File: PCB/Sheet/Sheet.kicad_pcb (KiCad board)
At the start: 2 copper layers, 36 x 32.4 mm, 4 parts, among them U1 MCP9700Ax-ELT, U2 MCP2562-E-MF, U3 ATtiny1616-M, U6 MCP2515-xST

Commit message: Update Sheet.kicad_pcb
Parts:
- added R1: R_0201_0603Metric, Resistor_SMD:R_0201_0603Metric, F.Cu at (172.8, 104.6)
- added R2: R_0201_0603Metric, Resistor_SMD:R_0201_0603Metric, F.Cu at (191.1, 104.5)
- added R3: R_0201_0603Metric, Resistor_SMD:R_0201_0603Metric, F.Cu at (193.3, 115.7)
- added R4: R_0201_0603Metric, Resistor_SMD:R_0201_0603Metric, F.Cu at (178.1, 126.5)
- added R5: R_0201_0603Metric, Resistor_SMD:R_0201_0603Metric, F.Cu at (170.5, 116.3)
- added R6: R_0201_0603Metric, Resistor_SMD:R_0201_0603Metric, F.Cu at (181.4, 109.0)
- added adxl335-: Analog_LGA-16_3.25x3mm_P0.5mm_LayoutBorder3x5y, Sensor_Motion:Analog_LGA-16_3.25x3mm_P0.5mm_LayoutBorder3x5y, F.Cu at (177.4, 111.0)
- moved U2 19.6 mm to (193.5, 108.2)
- moved U1 1.85 mm to (190.6, 119.8), turned to 180 degrees
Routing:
- net (no net): track 0.00 -> 208.9 mm, vias 0 -> 6
- net Net-(U1-GND): track 0.00 -> 35.8 mm, vias 0 -> 2
- net Net-(U1-V_{DD}): track 0.00 -> 32.7 mm
- net Net-(U2-RXD): track 0.00 -> 24.4 mm, vias 0 -> 2
- net Net-(U2-TXD): track 0.00 -> 8.92 mm
- net Net-(U1-V_{OUT}): track 0.00 -> 8.76 mm, vias 0 -> 2
- net unconnected-(U2-CANH-Pad7): track 0.00 -> 0.94 mm, vias 0 -> 1
- net unconnected-(U2-CANL-Pad6): track 0.00 -> 0.91 mm, vias 0 -> 1

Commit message: PCB design
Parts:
- removed adxl335-: Analog_LGA-16_3.25x3mm_P0.5mm_LayoutBorder3x5y, Sensor_Motion:Analog_LGA-16_3.25x3mm_P0.5mm_LayoutBorder3x5y
- added C1: C_0402_1005Metric_Pad0.74x0.62mm_HandSolder, Capacitor_SMD:C_0402_1005Metric_Pad0.74x0.62mm_HandSolder, F.Cu at (183.4, 118.3)
- added C2: C_0402_1005Metric_Pad0.74x0.62mm_HandSolder, Capacitor_SMD:C_0402_1005Metric_Pad0.74x0.62mm_HandSolder, F.Cu at (183.4, 119.3)
- added C3: C_0402_1005Metric_Pad0.74x0.62mm_HandSolder, Capacitor_SMD:C_0402_1005Metric_Pad0.74x0.62mm_HandSolder, F.Cu at (183.4, 120.3)
- added Diode: D_0201_0603Metric, Diode_SMD:D_0201_0603Metric, F.Cu at (176.6, 108.0)
- added IC1: ADXL33X, 16LCSP, F.Cu at (187.6, 116.8)
- added LED: LED_1206_3216Metric, LED_SMD:LED_1206_3216Metric, F.Cu at (174.1, 118.6)
- added LED: LED_1206_3216Metric, LED_SMD:LED_1206_3216Metric, F.Cu at (191.3, 119.6)
- added LED: LED_1206_3216Metric, LED_SMD:LED_1206_3216Metric, F.Cu at (181.9, 124.3)
- added LED: LED_1206_3216Metric, LED_SMD:LED_1206_3216Metric, F.Cu at (173.4, 108.3)
- added LEDs: SolderJumper-2_P1.3mm_Bridged2Bar_RoundedPad1.0x1.5mm, Jumper:SolderJumper-2_P1.3mm_Bridged2Bar_RoundedPad1.0x1.5mm, F.Cu at (176.5, 109.3)
- added PROG: PinHeader_1x04_P1.00mm_Vertical, Connector_PinHeader_1.00mm:PinHeader_1x04_P1.00mm_Vertical, F.Cu at (177.1, 115.2)
- added R7: R_0201_0603Metric, Resistor_SMD:R_0201_0603Metric, F.Cu at (187.1, 120.5)
- moved R2 9.51 mm to (190.2, 114.0)
- moved U1 8.42 mm to (193.1, 111.8), turned to 0 degrees
- moved R6 0.73 mm to (181.5, 109.7)
- moved U6 0.71 mm to (181.5, 102.6), turned to 0 degrees
- moved U2 0.16 mm to (193.3, 108.2)
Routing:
- net Net-(D1-K): track 35.8 -> 336.2 mm, vias 2 -> 40
- net Net-(U1-V_{DD}): track 32.7 -> 223.5 mm, vias 0 -> 19
- net unconnected-(U2-CANH-Pad7): track 0.94 -> 152.1 mm, vias 1 -> 14
- net Net-(U2-RXD): track 24.4 -> 154.0 mm, vias 2 -> 8
- net (no net): track 208.9 -> 251.2 mm, vias 6 -> 2
- net Net-(U3-PB3): track 0.00 -> 19.7 mm, vias 0 -> 2
- net unconnected-(U3-~{RESET}/PA0-Pad19): track 0.00 -> 18.4 mm, vias 0 -> 1
- net Net-(U3-PA4): track 0.00 -> 18.1 mm, vias 0 -> 2
- net Net-(U3-PB5): track 0.00 -> 16.2 mm, vias 0 -> 2
- net Net-(U3-PA2): track 0.00 -> 16.1 mm
- net Net-(U3-PB4): track 0.00 -> 16.1 mm, vias 0 -> 2
- net Net-(U2-TXD): track 8.92 -> 21.4 mm, vias 0 -> 2
- net Net-(U3-PA3): track 0.00 -> 12.3 mm, vias 0 -> 4
- net Net-(U3-PA1): track 0.00 -> 11.3 mm, vias 0 -> 2
- net unconnected-(U2-CANL-Pad6): track 0.91 -> 3.11 mm
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
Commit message: images and updates
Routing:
- net Net-(D1-K): track 336.2 -> 356.3 mm, vias 40 -> 42
- net (no net): track 251.2 -> 244.4 mm
- net Net-(U1-V_{DD}): track 223.5 -> 227.8 mm
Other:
- outline, holes or cut-outs redrawn

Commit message: updates
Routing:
- net Net-(U1-V_{DD}): track 227.8 -> 236.2 mm
- net Net-(D1-K): track 356.3 -> 353.7 mm
- net (no net): track 244.4 -> 242.6 mm
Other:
- board text added: "TACSHEET Tactile sensor array"

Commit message: PCB updates
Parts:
- added CR: 120, Resistor_SMD:R_0201_0603Metric, F.Cu at (196.1, 109.7)
- added crystal: Crystal_SMD_2012-2Pin_2.0x1.2mm, Crystal:Crystal_SMD_2012-2Pin_2.0x1.2mm, F.Cu at (175.9, 99.8)
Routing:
- net (no net): track 242.6 -> 208.7 mm, vias 2 -> 3
- net Net-(U1-V_{DD}): track 236.2 -> 261.2 mm
- net Net-(D1-K): track 353.7 -> 363.0 mm
- net unconnected-(U6-OSC1-Pad9): track 0.00 -> 9.24 mm
- net unconnected-(U6-OSC2-Pad8): track 0.00 -> 5.45 mm
- net unconnected-(U2-CANL-Pad6): track 3.11 -> 5.37 mm
- net unconnected-(U2-CANH-Pad7): track 152.1 -> 154.2 mm, vias 14 -> 15

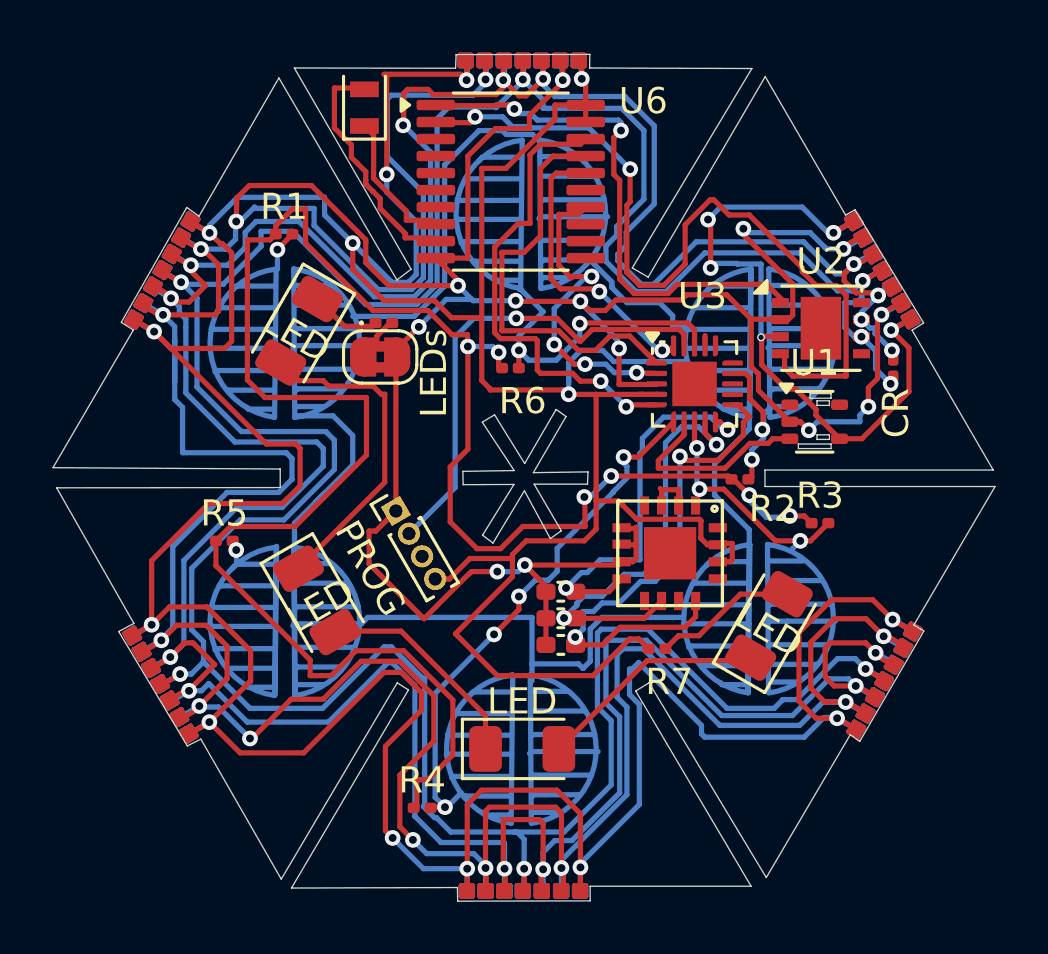
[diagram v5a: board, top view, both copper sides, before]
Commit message: INtegration of multiplexer
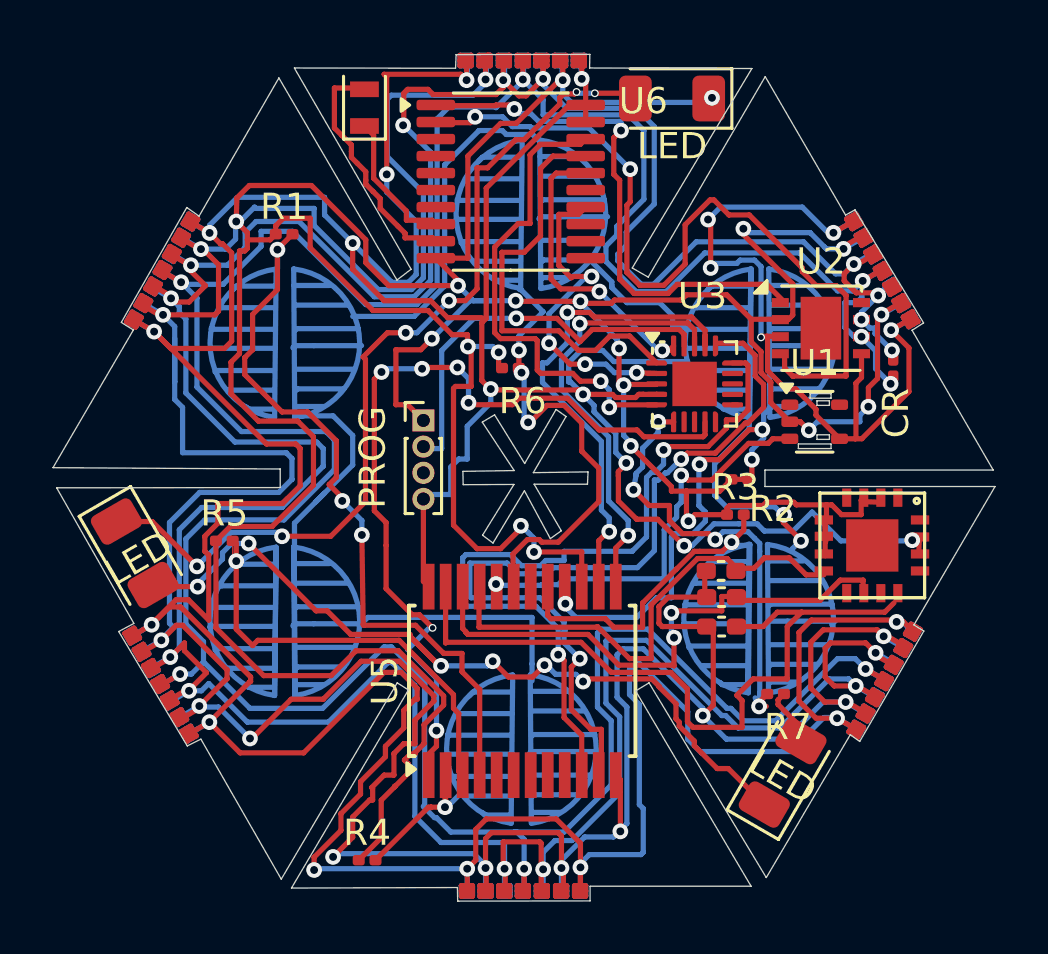
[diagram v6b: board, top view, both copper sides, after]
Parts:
- removed Diode: D_0201_0603Metric, Diode_SMD:D_0201_0603Metric
- removed the LED at (173.4, 108.3)
- removed LEDs: SolderJumper-2_P1.3mm_Bridged2Bar_RoundedPad1.0x1.5mm, Jumper:SolderJumper-2_P1.3mm_Bridged2Bar_RoundedPad1.0x1.5mm
- added U5: CD74HC4067SM, Package_SO:SSOP-24_5.3x8.2mm_P0.65mm, F.Cu at (181.9, 121.7)
- moved LED 25.5 mm to (187.7, 99.4), turned to 180 degrees
- moved IC1 7.73 mm to (195.3, 116.5)
- moved LED 7.18 mm to (167.1, 116.8)
- moved C2 6.20 mm to (189.5, 118.5)
- moved C3 6.18 mm to (189.5, 119.6)
- moved C1 6.18 mm to (189.5, 117.5)
- moved LED 5.64 mm to (191.9, 125.2)
- moved R7 4.85 mm to (191.6, 122.2)
- moved PROG 3.61 mm to (178.2, 111.7), turned to 0 degrees
- moved R3 3.25 mm to (190.1, 115.3)
- moved R4 2.90 mm to (176.0, 128.5)
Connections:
- U1 pad 2: Net-(D1-K) -> Net-(D3-K)
- U2 pad 2: Net-(D1-K) -> Net-(U2-VSS)
- U2 pad 5: unconnected-(U2-Vio-Pad5) -> Net-(U1-V_{DD})
- U2 pad 6: unconnected-(U2-CANL-Pad6) -> Net-(U2-CANL)
- U2 pad 7: unconnected-(U2-CANH-Pad7) -> Net-(U2-CANH)
- U3 pad 10: Net-(U3-PB4) -> unconnected-(U3-PB4-Pad10)
- U3 pad 11: Net-(U3-PB3) -> unconnected-(U3-PB3-Pad11)
- U3 pad 14: Net-(D1-K) -> unconnected-(U3-PB0-Pad14)
- U3 pad 15: unconnected-(U3-PC0-Pad15) -> Net-(U3-PC0)
- U3 pad 16: Net-(D1-K) -> Net-(U3-PC1)
- U3 pad 17: Net-(D1-K) -> Net-(U3-PC2)
- U3 pad 18: Net-(D1-K) -> Net-(U3-PC3)
- U3 pad 21: Net-(D1-K) -> Net-(D3-K)
- U3 pad 3: Net-(D1-K) -> Net-(D3-K)
- U3 pad 4: Net-(U1-V_{DD}) -> Net-(U3-VCC)
- U3 pad 6: Net-(D1-K) -> Net-(U3-PA5)
- U3 pad 7: Net-(U1-V_{OUT}) -> unconnected-(U3-PA6-Pad7)
- U3 pad 8: Net-(D1-K) -> unconnected-(U3-PA7-Pad8)
- U6 pad 10: Net-(D1-K) -> Net-(U2-VSS)
- U6 pad 8: unconnected-(U6-OSC2-Pad8) -> Net-(U6-OSC2)
- U6 pad 9: unconnected-(U6-OSC1-Pad9) -> Net-(U6-OSC1)
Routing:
- net Net-(D1-K): track 363.0 -> 0.00 mm, vias 42 -> 0
- net (no net): track 208.7 -> 480.2 mm, vias 3 -> 2
- net unconnected-(U2-CANH-Pad7): track 154.2 -> 0.00 mm, vias 15 -> 0
- net Net-(U2-CANH): track 0.00 -> 153.3 mm, vias 0 -> 15
- net Net-(U3-PC1): track 0.00 -> 64.5 mm, vias 0 -> 8
- net Net-(U1-V_{DD}): track 261.2 -> 291.9 mm, vias 19 -> 29
- net Net-(U3-PC0): track 0.00 -> 29.7 mm, vias 0 -> 2
- net Net-(U5-I5): track 0.00 -> 28.5 mm, vias 0 -> 3
- net Net-(U4-XOUT): track 0.00 -> 28.2 mm
- net Net-(U4-YOUT): track 0.00 -> 21.3 mm, vias 0 -> 2
- net Net-(U3-PB3): track 19.7 -> 0.00 mm, vias 2 -> 0
- net Net-(U3-PC2): track 0.00 -> 19.0 mm, vias 0 -> 2
- net Net-(U5-I6): track 0.00 -> 18.8 mm, vias 0 -> 1
- net Net-(U4-ZOUT): track 0.00 -> 18.1 mm
- net Net-(U5-I7): track 0.00 -> 17.7 mm, vias 0 -> 1
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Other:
- board text added: "D1"

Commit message: Update Sheet.kicad_pcb
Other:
- board text added: "Designed by Dexter Shepherd"
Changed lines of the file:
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@@
   (gr_line (start 166.51 119.79) (end 167.09 119.48)
     (stroke (width 0.05) (type default)) (layer "Edge.Cuts"))
-  (gr_text "TACSHEET\nTactile sensor array" (at 187.725 120.675) (layer "B.SilkS")
+  (gr_text "Designed by\nDexter Shepherd" (at 197.625 113.3) (layer "B.SilkS")
+    (effects (font (size 0.5 0.5) (thickness 0.1)) (justify left bottom mirror))
+  )
+  (gr_text "TACSHEET\nTactile sensor\narray" (at 186.525 121.35) (layer "B.SilkS")
     (effects (font (size 1 1) (thickness 0.1)) (justify left bottom mirror))
   )

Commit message: files
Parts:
- removed C2: C_0402_1005Metric_Pad0.74x0.62mm_HandSolder, Capacitor_SMD:C_0402_1005Metric_Pad0.74x0.62mm_HandSolder
- removed LED (x3): LED_1206_3216Metric, LED_SMD:LED_1206_3216Metric
- added C1A: C_0402_1005Metric_Pad0.74x0.62mm_HandSolder, Capacitor_SMD:C_0402_1005Metric_Pad0.74x0.62mm_HandSolder, F.Cu at (178.6, 94.9)
- added C2A: C_0402_1005Metric_Pad0.74x0.62mm_HandSolder, Capacitor_SMD:C_0402_1005Metric_Pad0.74x0.62mm_HandSolder, F.Cu at (178.6, 95.9)
- added C3A: C_0402_1005Metric_Pad0.74x0.62mm_HandSolder, Capacitor_SMD:C_0402_1005Metric_Pad0.74x0.62mm_HandSolder, F.Cu at (178.6, 97.1)
- added JST: JST_ACH_BM04B-ACHSS-A-GAN-ETF_1x04-1MP_P1.20mm_Vertical, Connector_JST:JST_ACH_BM04B-ACHSS-A-GAN-ETF_1x04-1MP_P1.20mm_Vertical, F.Cu at (162.6, 85.7)
- added LED1: LED_1206_3216Metric, LED_SMD:LED_1206_3216Metric, F.Cu at (180.9, 102.6)
- added LED2: LED_1206_3216Metric, LED_SMD:LED_1206_3216Metric, F.Cu at (156.2, 94.3)
- added LED3: LED_1206_3216Metric, LED_SMD:LED_1206_3216Metric, F.Cu at (176.7, 76.9)
- added R10: R_0201_0603Metric, Resistor_SMD:R_0201_0603Metric, F.Cu at (155.8, 77.7)
- added R11: R_0201_0603Metric, Resistor_SMD:R_0201_0603Metric, F.Cu at (195.2, 77.6)
- added R12: R_0201_0603Metric, Resistor_SMD:R_0201_0603Metric, F.Cu at (165.9, 109.5)
- added U7: DRV5055A1xDBZxQ1, Package_TO_SOT_SMD:SOT-23, F.Cu at (162.4, 95.5)
- added U8: DRV5055A1xDBZxQ1, Package_TO_SOT_SMD:SOT-23, F.Cu at (176.8, 105.6)
- C1, C3: value C_0402_1005Metric_Pad0.74x0.62mm_HandSolder -> C_0402_1005Metric; footprint Capacitor_SMD:C_0402_1005Metric_Pad0.74x0.62mm_HandSolder -> Capacitor_SMD:C_0402_1005Metric
- moved C3 42.5 mm to (176.7, 79.1), turned to 90 degrees
- moved R1 26.5 mm to (161.7, 80.5)
- moved CR 25.1 mm to (185.2, 87.2)
- moved IC1 25.1 mm to (184.4, 94.0)
- moved PROG 25.1 mm to (167.2, 89.2)
- moved R2 25.1 mm to (179.3, 91.4)
- moved R3 25.1 mm to (179.1, 92.8)
- moved R4 25.1 mm to (165.1, 106.0)
- moved R5 25.1 mm to (159.6, 93.8)
- moved R6 25.1 mm to (170.5, 87.2)
- moved R7 25.1 mm to (180.7, 99.6)
- moved U1 25.1 mm to (182.2, 89.2)
- moved U2 25.1 mm to (182.4, 85.7)
- moved U3 25.1 mm to (177.6, 87.8)
- moved U5 25.1 mm to (171.0, 99.1)
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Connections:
- U1 pad 1: unconnected-(U1-NC-Pad1) -> (no net)
- U1 pad 2: Net-(D3-K) -> (no net)
- U1 pad 3: Net-(U1-V_{OUT}) -> (no net)
- U1 pad 4: Net-(U1-V_{DD}) -> (no net)
- U1 pad 5: unconnected-(U1-NC-Pad5) -> (no net)
- U2 pad 1: Net-(U2-TXD) -> (no net)
- U2 pad 2: Net-(U2-VSS) -> (no net)
- U2 pad 3: Net-(U1-V_{DD}) -> (no net)
- U2 pad 4: Net-(U2-RXD) -> (no net)
- U2 pad 5: Net-(U1-V_{DD}) -> (no net)
- U2 pad 6: Net-(U2-CANL) -> (no net)
- U2 pad 7: Net-(U2-CANH) -> (no net)
- U2 pad 8: unconnected-(U2-SHDN-Pad8) -> (no net)
- U2 pad 9: unconnected-(U2-PAD-Pad9) -> (no net)
- U3 pad 1: Net-(U3-PA2) -> (no net)
- U3 pad 10: unconnected-(U3-PB4-Pad10) -> (no net)
- U3 pad 11: unconnected-(U3-PB3-Pad11) -> (no net)
- U3 pad 12: unconnected-(U3-PB2-Pad12) -> (no net)
- U3 pad 13: unconnected-(U3-PB1-Pad13) -> (no net)
- U3 pad 14: unconnected-(U3-PB0-Pad14) -> (no net)
- U3 pad 15: Net-(U3-PC0) -> (no net)
- U3 pad 16: Net-(U3-PC1) -> (no net)
- U3 pad 17: Net-(U3-PC2) -> (no net)
- U3 pad 18: Net-(U3-PC3) -> (no net)
- U3 pad 19: unconnected-(U3-~{RESET}/PA0-Pad19) -> (no net)
- U3 pad 2: Net-(U3-PA3) -> (no net)
- U3 pad 20: Net-(U3-PA1) -> (no net)
- U3 pad 21: Net-(D3-K) -> (no net)
- U3 pad 3: Net-(D3-K) -> (no net)
- U3 pad 4: Net-(U3-VCC) -> (no net)
- U3 pad 5: Net-(U3-PA4) -> (no net)
- U3 pad 6: Net-(U3-PA5) -> (no net)
- U3 pad 7: unconnected-(U3-PA6-Pad7) -> (no net)
- U3 pad 8: unconnected-(U3-PA7-Pad8) -> (no net)
- U3 pad 9: Net-(U3-PB5) -> (no net)
- U5 pad 1: Net-(U3-PB5) -> (no net)
- U5 pad 10: Net-(U3-PC0) -> (no net)
- U5 pad 11: Net-(U3-PC1) -> (no net)
- U5 pad 12: Net-(U2-VSS) -> (no net)
- U5 pad 13: Net-(U3-PC3) -> (no net)
- U5 pad 14: Net-(U3-PC2) -> (no net)
- U5 pad 15: Net-(U2-VSS) -> (no net)
- U5 pad 16: Net-(U5-I15) -> (no net)
- U5 pad 17: Net-(U5-I14) -> (no net)
- U5 pad 18: unconnected-(U5-I13-Pad18) -> (no net)
- U5 pad 19: Net-(U5-I12) -> (no net)
- U5 pad 2: Net-(U5-I7) -> (no net)
- U5 pad 20: Net-(U1-V_{OUT}) -> (no net)
- U5 pad 21: Net-(U4-ZOUT) -> (no net)
- U5 pad 22: Net-(U4-YOUT) -> (no net)
- U5 pad 23: Net-(U4-XOUT) -> (no net)
- U5 pad 24: Net-(U1-V_{DD}) -> (no net)
- U5 pad 3: Net-(U5-I6) -> (no net)
- U5 pad 4: Net-(U5-I5) -> (no net)
- U5 pad 5: unconnected-(U5-I4-Pad5) -> (no net)
- U5 pad 6: unconnected-(U5-I3-Pad6) -> (no net)
- U5 pad 7: unconnected-(U5-I2-Pad7) -> (no net)
- U5 pad 8: unconnected-(U5-I1-Pad8) -> (no net)
- U5 pad 9: unconnected-(U5-I0-Pad9) -> (no net)
- U6 pad 1: Net-(U2-TXD) -> (no net)
- U6 pad 10: Net-(U2-VSS) -> (no net)
- U6 pad 11: unconnected-(U6-~{RX1BF}-Pad11) -> (no net)
- U6 pad 12: unconnected-(U6-~{RX0BF}-Pad12) -> (no net)
- U6 pad 13: unconnected-(U6-~{INT}-Pad13) -> (no net)
- U6 pad 14: Net-(U3-PA3) -> (no net)
- U6 pad 15: unconnected-(U6-NC-Pad15) -> (no net)
- U6 pad 16: Net-(U3-PA1) -> (no net)
- U6 pad 17: Net-(U3-PA2) -> (no net)
- U6 pad 18: Net-(U3-PA4) -> (no net)
- U6 pad 19: unconnected-(U6-~{RESET}-Pad19) -> (no net)
- U6 pad 2: Net-(U2-RXD) -> (no net)
- U6 pad 20: Net-(U1-V_{DD}) -> (no net)
- U6 pad 3: unconnected-(U6-CLKOUT/SOF-Pad3) -> (no net)
- U6 pad 4: unconnected-(U6-~{TX0RTS}-Pad4) -> (no net)
- U6 pad 5: unconnected-(U6-~{TX1RTS}-Pad5) -> (no net)
- U6 pad 6: unconnected-(U6-NC-Pad6) -> (no net)
- U6 pad 7: unconnected-(U6-~{TX2RTS}-Pad7) -> (no net)
- U6 pad 8: Net-(U6-OSC2) -> (no net)
- U6 pad 9: Net-(U6-OSC1) -> (no net)
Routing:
- net (no net): track 480.2 -> 1925.3 mm, vias 2 -> 163
- net Net-(U1-V_{DD}): track 291.9 -> 0.00 mm, vias 29 -> 0
- net Net-(U2-RXD): track 162.5 -> 0.00 mm, vias 10 -> 0
- net Net-(U2-CANH): track 153.3 -> 0.00 mm, vias 15 -> 0
- net Net-(U3-PC1): track 64.5 -> 0.00 mm, vias 8 -> 0
- net Net-(U3-PB5): track 32.5 -> 0.00 mm, vias 6 -> 0
- net Net-(U3-PC0): track 29.7 -> 0.00 mm, vias 2 -> 0
- net Net-(U5-I5): track 28.5 -> 0.00 mm, vias 3 -> 0
- net Net-(U4-XOUT): track 28.2 -> 0.00 mm
- net Net-(U2-TXD): track 21.4 -> 0.00 mm, vias 2 -> 0
- net Net-(U4-YOUT): track 21.3 -> 0.00 mm, vias 2 -> 0
- net Net-(U3-PC2): track 19.0 -> 0.00 mm, vias 2 -> 0
- net Net-(U5-I6): track 18.8 -> 0.00 mm, vias 1 -> 0
- net Net-(U3-PA4): track 18.5 -> 0.00 mm, vias 2 -> 0
- net Net-(U4-ZOUT): track 18.1 -> 0.00 mm
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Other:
- board size 36 x 32.4 mm -> 54.8 x 47.7 mm
